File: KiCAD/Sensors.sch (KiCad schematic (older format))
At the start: 15 parts, among them Q2 BSS138, Q3 BSS138, U10 DLHR-L10D-E1BD-C-NAV8, U11 DLHR-L10D-E1BD-C-NAV8, U12 DLHR-L10D-E1BD-C-NAV8, U4 HSCDANN015PA2A5, U5 DLHR-L10D-E1BD-C-NAV8, U6 DLHR-L10D-E1BD-C-NAV8, U7 DLHR-L10D-E1BD-C-NAV8, U8 DLHR-L10D-E1BD-C-NAV8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

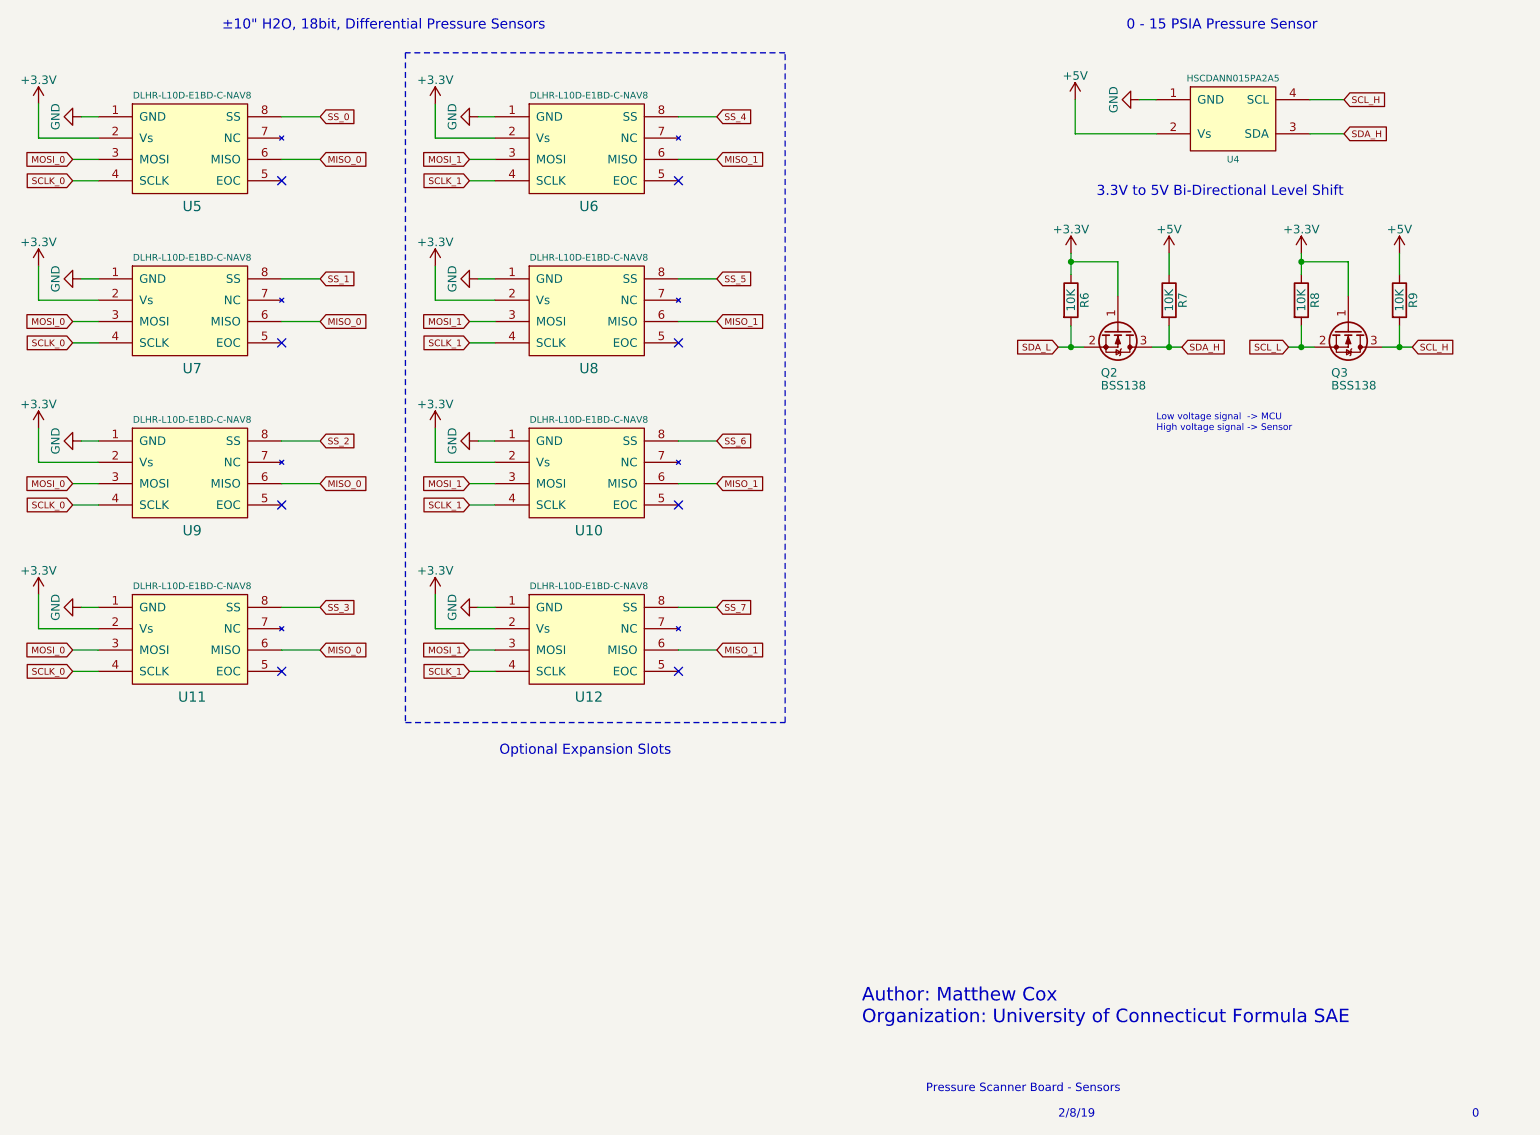
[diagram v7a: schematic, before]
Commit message: Dropped 4 spare sensors, revising layout.
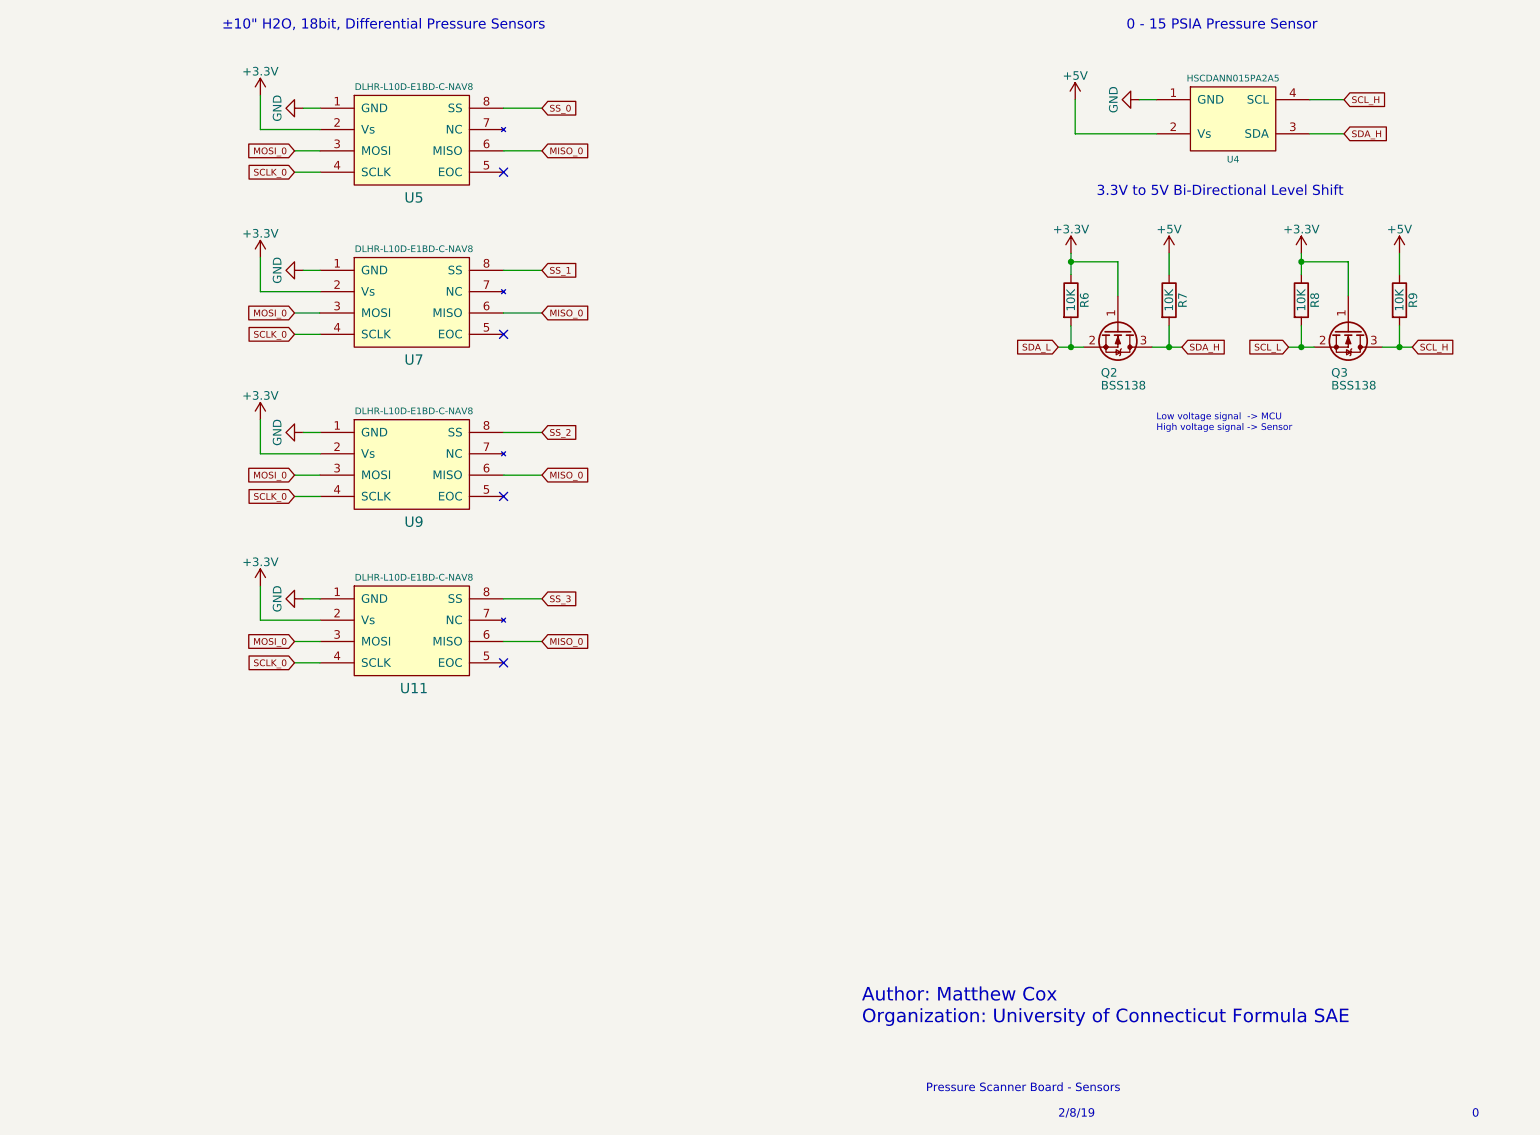
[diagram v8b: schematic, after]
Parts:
- removed U10, U12, U6, U8: DLHR-L10D-E1BD-C-NAV8, DLHR-L10D-E1BD-C-NAV8:DLHR-L10D-E1BD-C-NAV8, symbol DLHR-L10D-E1BD-C-NAV8
- R6, R7, R8, R9: footprint Resistors_SMD:R_1210 -> Resistors_SMD:R_0603
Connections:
- no-connect marks 8 -> 4
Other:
- note removed: "Optional Expansion Slots"
- moved on the sheet: U11, U5, U7, U9
